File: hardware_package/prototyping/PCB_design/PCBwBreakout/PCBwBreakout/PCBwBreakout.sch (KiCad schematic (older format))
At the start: 18 parts

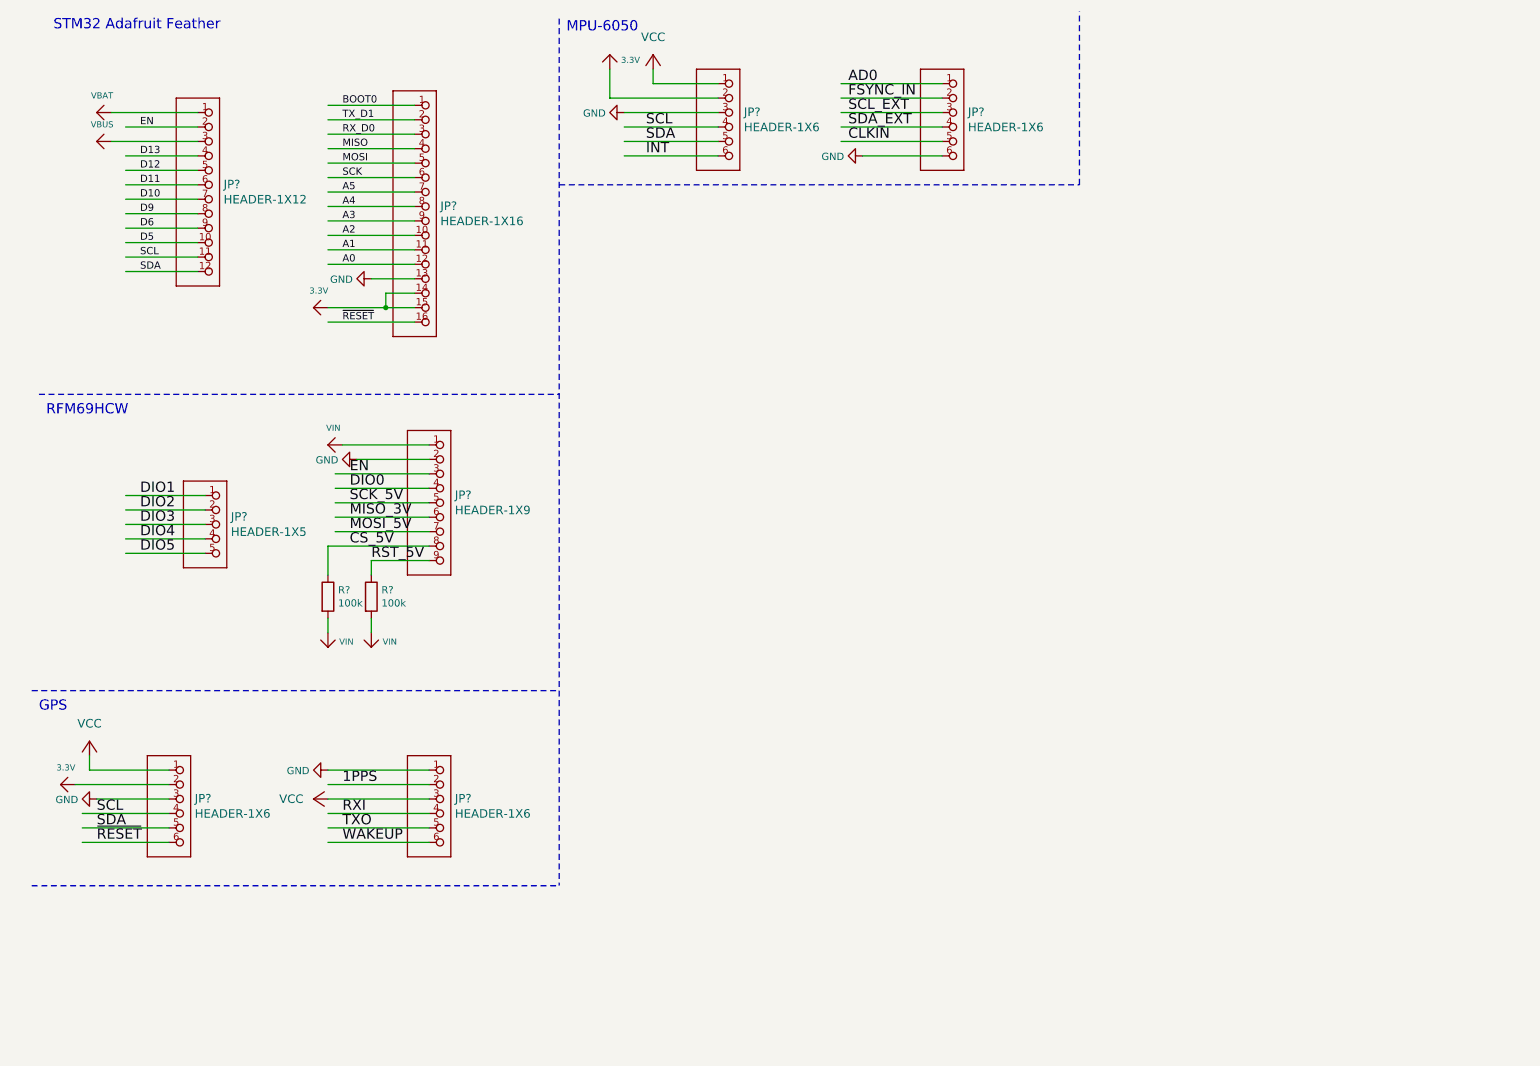
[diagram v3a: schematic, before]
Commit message: Added MP3115A2 Header, made custom 1X7 Header symbol
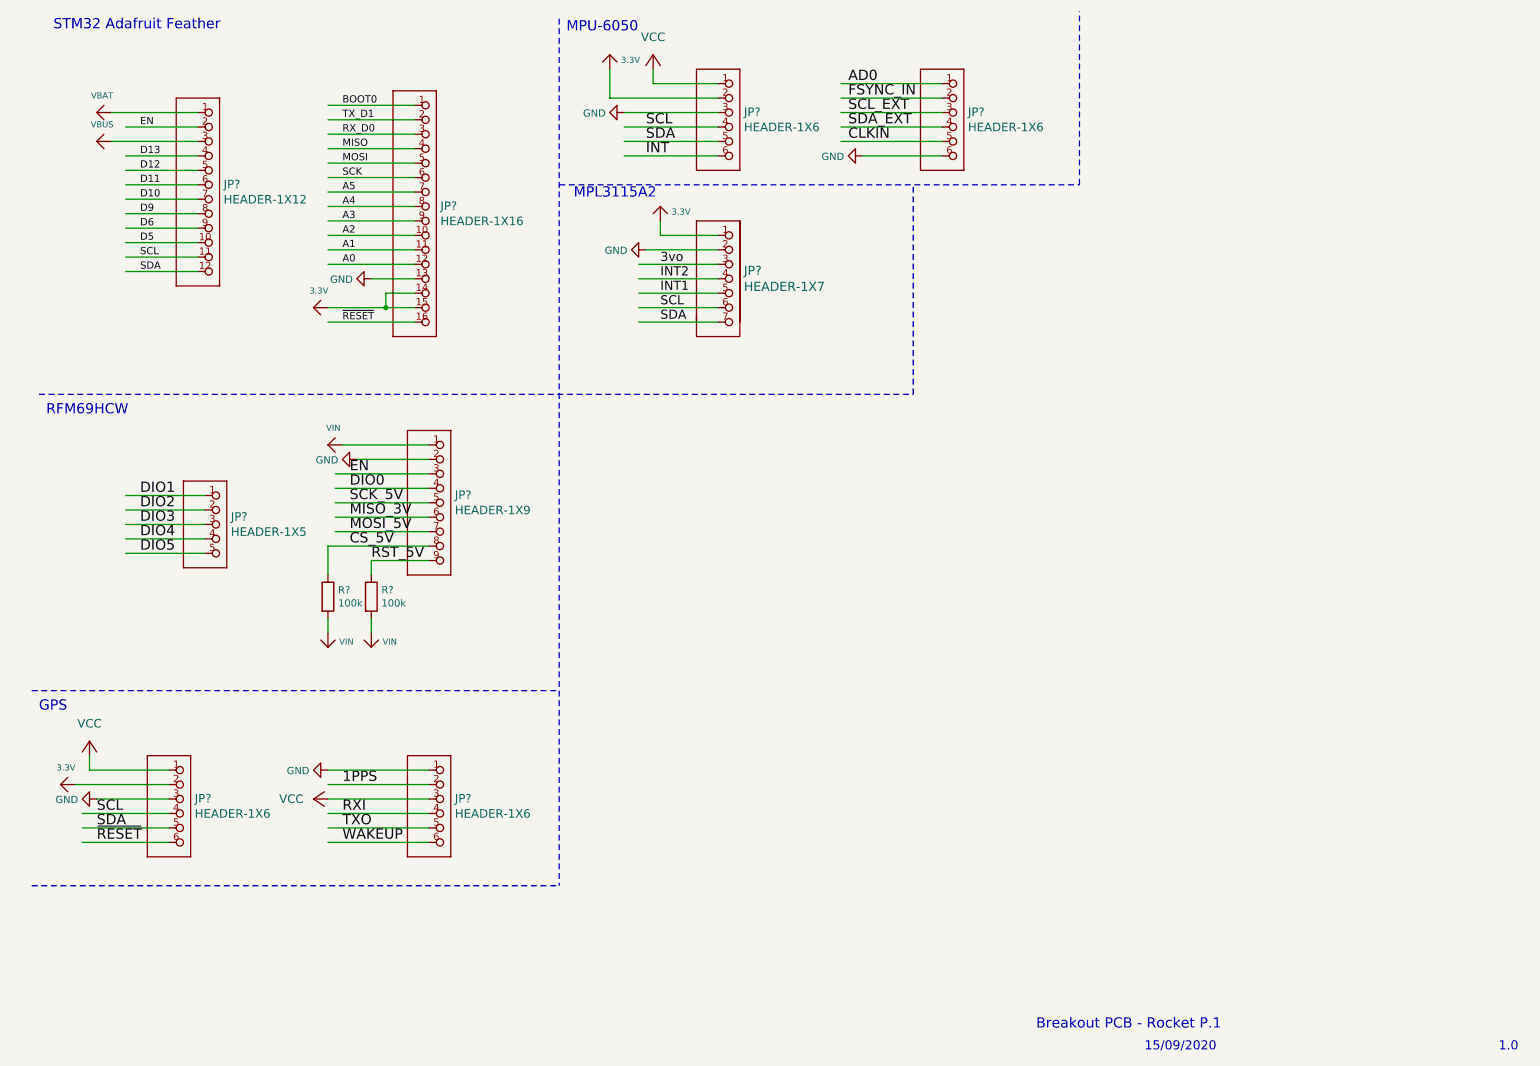
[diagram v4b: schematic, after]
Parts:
- added ?: 3.3V, symbol PCBwBreakout-eagle-import:3.3V
- added JP?: HEADER-1X7, symbol PCBwBreakout-eagle-import:HEADER-1X7
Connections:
- net labels added: 3vo, INT1, INT2
- wire segments 75 -> 83
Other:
- note added: "1.0\n"
- note added: "15/09/2020\n"
- note added: "Breakout PCB - Rocket P.1"
- note added: "MPL3115A2\n"
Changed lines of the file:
@@
 Text Label 1200 2250 0    50   ~ 0
 SDA
-Wire Notes Line
-	500  3100 4100 3100
 Text Notes 600  700  0    71   ~ 0
 STM32 Adafruit Feather\n\n
@@
 Text Notes 4150 600  0    71   ~ 0
 MPU-6050\n
+Text Notes 7400 7500 0    71   ~ 0
+Breakout PCB - Rocket P.1
+Text Notes 8150 7650 0    63   ~ 0
+15/09/2020\n
+Text Notes 10600 7650 0    63   ~ 0
+1.0\n
+$Comp
+L PCBwBreakout-eagle-import:HEADER-1X7 JP?
+U 1 1 5F6FE755
+P 5250 2850
+F 0 "JP?" H 5378 3456 63  0000 L CNN
+F 1 "HEADER-1X7" H 5378 3345 63  0000 L CNN
+F 2 "" H 5250 2850 63  0001 C CNN
+F 3 "" H 5250 2850 63  0001 C CNN
+	1    5250 2850
+	1    0    0    -1
+$EndComp
+$Comp
+L PCBwBreakout-eagle-import:3.3V ?
+U 1 1 5F700307
+P 4800 1800
+F 0 "?" H 4850 1850 71  0001 C CNN
+F 1 "3.3V" H 4878 1763 42  0000 L CNN
+F 2 "" H 4800 1800 71  0001 C CNN
+F 3 "" H 4800 1800 71  0001 C CNN
+	1    4800 1800
+	1    0    0    -1
+$EndComp
+Wire Wire Line
+	4800 1900 4800 2000
+Wire Wire Line
+	4800 2000 5200 2000
+$Comp
+L power:GND #PWR?
+U 1 1 5F703624
+P 4700 2100
+F 0 "#PWR?" H 4700 1850 50  0001 C CNN
+F 1 "GND" V 4705 1972 50  0000 R CNN
+F 2 "" H 4700 2100 50  0001 C CNN
+F 3 "" H 4700 2100 50  0001 C CNN
+	1    4700 2100
+	0    1    1    0
+$EndComp
+Wire Wire Line
+	5200 2100 4700 2100
+Wire Wire Line
+	5200 2200 4650 2200
+Wire Wire Line
+	5200 2300 4650 2300
+Wire Wire Line
+	5200 2400 4650 2400
+Wire Wire Line
+	5200 2500 4650 2500
+Wire Wire Line
+	5200 2600 4650 2600
+Text Label 4800 2200 0    63   ~ 0
+3vo
+Text Label 4800 2300 0    63   ~ 0
+INT2
+Text Label 4800 2400 0    63   ~ 0
+INT1
+Text Label 4800 2500 0    63   ~ 0
+SCL
+Text Label 4800 2600 0    63   ~ 0
+SDA
+Wire Notes Line
+	6550 3100 6550 1650
+Wire Notes Line
+	500  3100 6550 3100
+Text Notes 4200 1750 0    71   ~ 0
+MPL3115A2\n
 $EndSCHEMATC
